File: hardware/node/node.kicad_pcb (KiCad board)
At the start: 4 copper layers, 48.5 x 50 mm, 68 parts, among them J1 BOOT0_Jumper, J2 FTDI, J3 SMA Female, J4 2 x AA, J5 SWD, Q1 Si2323DDS, SW1 DTSM-65R-V-B, U1 RFM69HW, U2 SHTC3, U3 AT25DF512C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

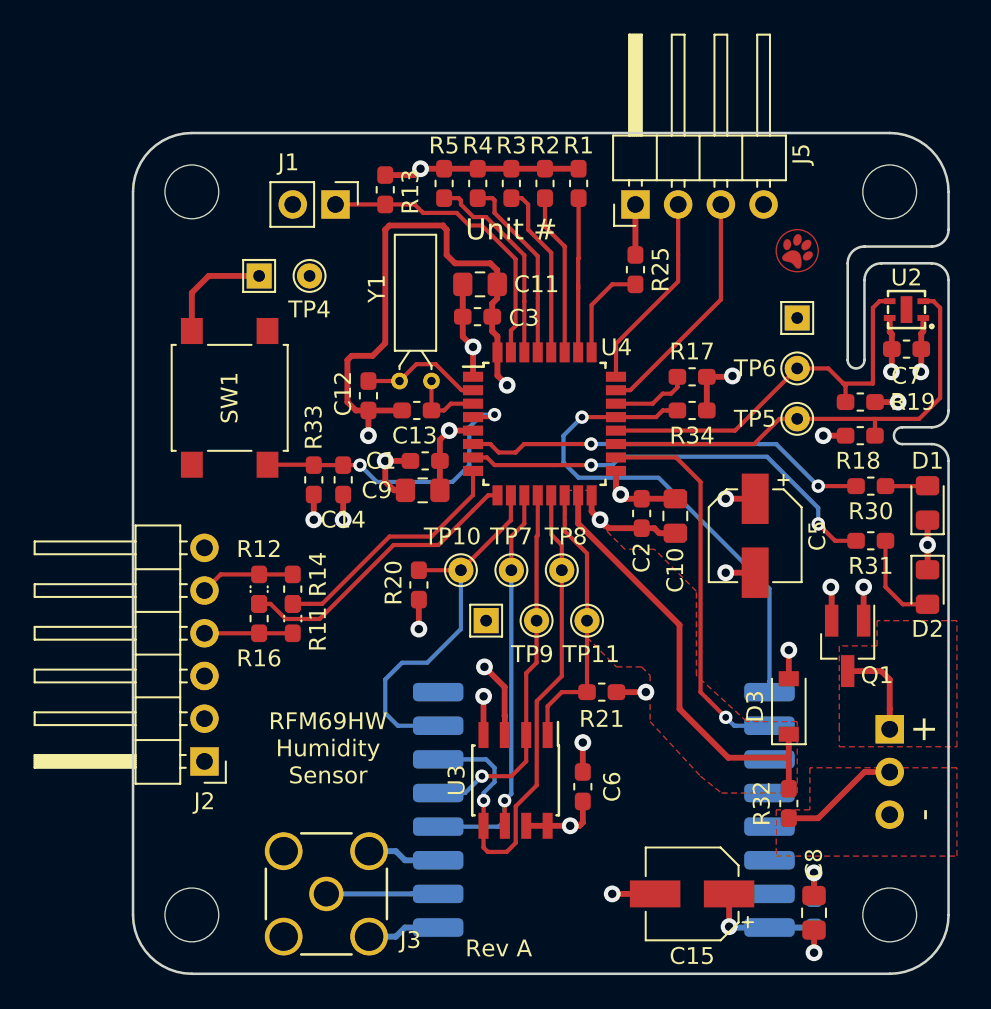
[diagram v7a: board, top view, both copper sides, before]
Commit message: Shortened SPI traces
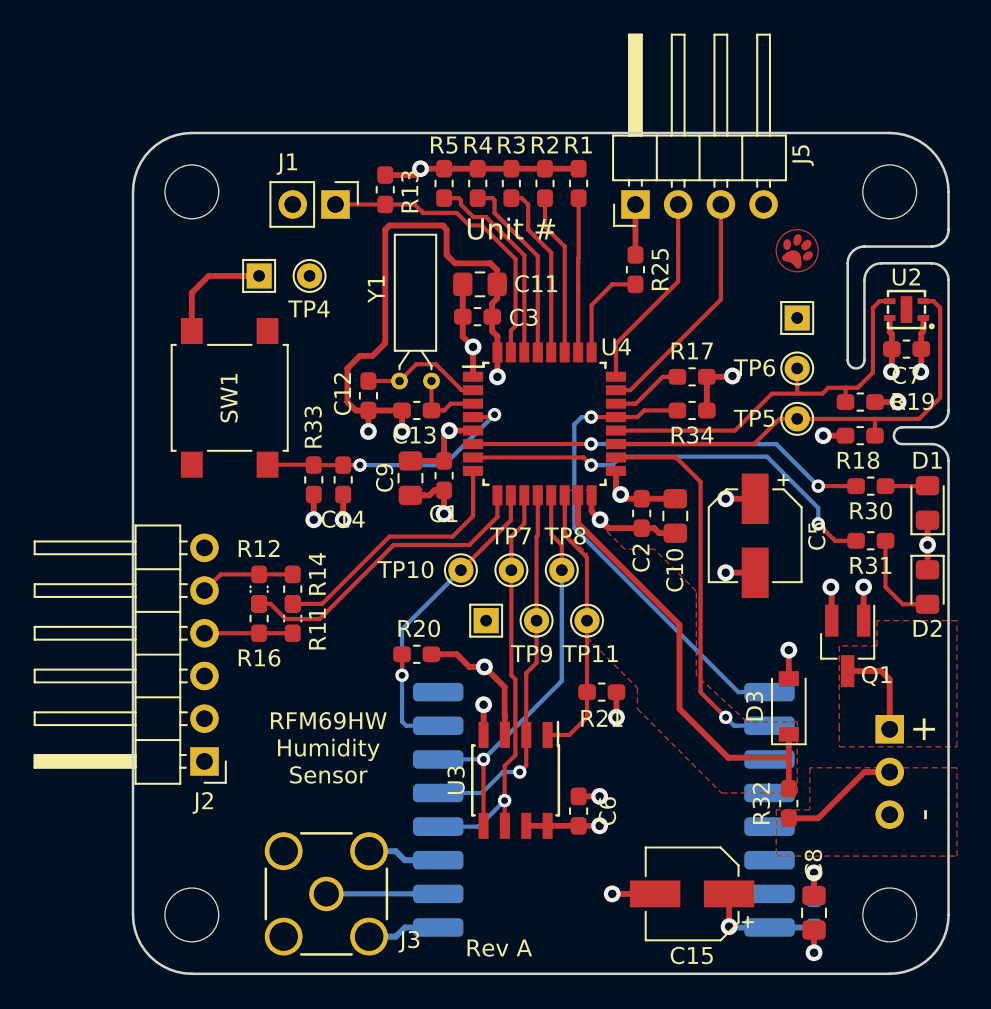
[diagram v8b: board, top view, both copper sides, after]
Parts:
- moved R20 4.13 mm to (73.4, 81.0), turned to 0 degrees
- moved C6 1.47 mm to (83.0, 90.3)
- moved C1 1.43 mm to (75.0, 70.4), turned to 90 degrees
- moved C9 1.03 mm to (73.0, 70.5), turned to 270 degrees
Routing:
- net /SPI1_MOSI: track 32.9 -> 24.6 mm
- net /CS_RFM69: track 22.9 -> 19.6 mm, vias 0 -> 1
- net /RFM69_RST: track 30.5 -> 28.3 mm
- net /STM_RESET: track 18.2 -> 16.1 mm
- net GND: track 126.4 -> 124.8 mm, vias 16 -> 17
- net VCC: track 49.8 -> 51.1 mm, vias 15 -> 14
- net /USART2_RX: track 17.6 -> 18.3 mm
- net /USART2_TX: track 14.8 -> 15.6 mm
- net /SPI1_SCK: track 25.4 -> 24.9 mm
